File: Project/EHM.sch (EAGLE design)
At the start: 111 parts, among them J1 282834-2, J2 282834-2, J3 282834-2, J4 282834-2, J5 S2B-PH-SM4-TB(LF)(SN), J6 S6B-PH-SM4-TB(LF)(SN), Q1 BC557B, Q2 BC547B, U1 MAX9934TAUA, U2 BQ25570RGRR, U3 TSU111ICT, U4 MAX9934TAUA, U5 TSU111ICT, U6 TSU111ICT

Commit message: Update project to v1.3
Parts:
- added J7: S2B-PH-SM4-TB(LF)(SN), S2B-PH-SM4-TB_LF__SN_:S2B-PH-SM4-TB(LF)(SN)
- C1: value DNP -> 0.01uF; device rcl:C-EUC1210 -> rcl:C-EUC0805
- C10: value (none) -> 0.1uF
- C11: value 0.01uF -> DNP
- C12: value 4.7uF -> 0.1uF
- C13, C9: value 0.1uF -> 4.7uF
- C14: value DNP -> 0.1uF
- C15: value 4.7uF -> DNP
- C17: value 0.1uF -> DNP
- C2, C3: value 0.01uF -> DNP; device rcl:C-EUC0805 -> rcl:C-EUC1210
- C21: value DNP -> 0.1uF; device rcl:C-EUC1812 -> rcl:C-EUC0805
- C22: device rcl:C-EUC0805 -> rcl:C-EUC1812
- C23: device rcl:C-EUC0805 -> rcl:C-EUC0603
- C24, C25: value (none) -> 0.1uF; device rcl:C-EUC0805 -> rcl:C-EUC0603
- C4: value 22uF -> 0.01uF
- C5: value 4.7uF -> 0.01uF
- C6: value 0.1uF -> 22uF
- C7: value DNP -> 4.7uF
- C8: value DNP -> 0.1uF; device rcl:C-EUC1210 -> rcl:C-EUC0805
- J5: value S2B-PH-SM4-TB(LF)(SN) -> 282834-2; device S2B-PH-SM4-TB_LF__SN_:S2B-PH-SM4-TB(LF)(SN) -> 282834-2:282834-2
- R1, R10, R12, R13, R5, R9: value DNP -> (none)
- R11, R3: value DNP -> (none); device rcl:R-EU_R0603 -> Y14870RXX000B9R:Y14870RXX000B9R
- R15, R16, R17, R18, R19, R22, R23: value (none) -> DNP
- R4: device Y14870RXX000B9R:Y14870RXX000B9R -> rcl:R-EU_R0603
- R8: value (none) -> DNP; device Y14870RXX000B9R:Y14870RXX000B9R -> rcl:R-EU_R0603
- SJ1, SJ3, SJ8: device jumper:SJ2W -> jumper:SJ
- SJ13, SJ14, SJ17: device jumper:SJ -> jumper:SJ2W
- TP18: value TPPAD1-13Y -> TPPAD1-13; device testpad:TPPAD1-13Y -> testpad:TPPAD1-13
- TP23: value TPPAD1-13Y -> TPB1,27; device testpad:TPPAD1-13Y -> testpad:TPB1,27
- U1: value MAX9934TAUA -> BQ25570RGRR; device MAX9934TAUA:MAX9934TAUA -> BQ25570RGRR:BQ25570RGRR
- U2: value BQ25570RGRR -> MAX9934TAUA; device BQ25570RGRR:BQ25570RGRR -> MAX9934TAUA:MAX9934TAUA
- U3: value TSU111ICT -> MAX9934TAUA; device TSU111ICT:TSU111ICT -> MAX9934TAUA:MAX9934TAUA
- U4: value MAX9934TAUA -> MAX9620; device MAX9934TAUA:MAX9934TAUA -> MAX9620:MAX9620
- U5, U6: value TSU111ICT -> MAX9620; device TSU111ICT:TSU111ICT -> MAX9620:MAX9620
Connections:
- removed net N$15 (its old number): R5.1, U3.IN-, U3.OUT
- removed net N$19: Q2.C, R10.2, R9.1
- new net N$25: Q2.C, R14.2, R15.1
- new net N$9: R18.1, U4.IN-, U4.OUT
- net CMES1: now also C2.1, C4.1, R1.2, U2.OUT; no longer C11.1, C8.1, R6.2, U4.OUT
- net CMES2: now also C5.1, U3.OUT; no longer C1.1, U1.OUT
- net GND: now also C10.1, C16.2, C17.2, C5.2, C6.2, C7.1, C8.1, C9.1, J5.1, J7.2, J7.SHIELD, R1.1, R13.1, R20.1, R5.1, U1.EP@1, U1.EP@2, U1.EP@3, U1.EP@4, U1.EP@5, U1.NC1, U1.NC2, U1.VSS@1, U1.VSS@2, U2.GROUND, U3.GROUND, U4.VCC-; no longer C10.2, C16.1, C17.1, C5.1, C6.1, C7.2, C8.2, C9.2, J5.2, J5.SHIELD, R12.1, R16.1, R23.1, R3.1, U1.GROUND, U2.EP@1, U2.EP@2, U2.EP@3, U2.EP@4, U2.EP@5, U2.NC1, U2.NC2, U2.VSS@1, U2.VSS@2, U3.VCC-, U4.GROUND
- net LBOOST: now also U1.LBOOST; no longer U2.LBOOST
- net LBUCK: now also U1.LBUCK; no longer U2.LBUCK
- net N$1: now also C18.1, SJ3.1, U2.RSN; no longer C22.1, SJ9.1, U4.RSN
- net N$10: now also C21.1, U3.RSP; no longer C20.1, U1.RSP
- net N$11: now also C19.1, U3.RSN; no longer C18.1, U1.RSN
- net N$12: now also R19.2; no longer C24.1, R20.2
- net N$13: now also R18.2, SJ17.3; no longer C25.1, R21.2, SJ19.3
- net N$14: now also SJ15.2, U4.IN+; no longer SJ12.2, U6.IN+
- net N$16: now also R21.2, SJ19.3; no longer C10.1, R5.2, SJ3.3
- net N$17: now also R16.2, R17.2, SJ14.1, U6.IN+; no longer R1.2, R3.2, SJ1.1, U3.IN+
- net N$18: now also R16.1, SJ14.3; no longer R1.1, SJ1.3
- net N$2: now also R20.2, R22.1; no longer R12.2, R13.1
- net N$20: now also R15.2; no longer R9.2
- net N$21: now also SJ13.3; no longer SJ8.3
- net N$23: now also R14.1; no longer R10.1
- net N$3: now also R22.2, R23.1; no longer R13.2, R14.1
- net N$4: now also R7.2, U2.CS; no longer R11.2, U4.CS
- net N$5: now also R19.1; no longer R20.1
- net N$6: now also C20.1, SJ5.1, U2.RSP; no longer C23.1, SJ10.1, U4.RSP
- net N$7: now also R8.2, U3.CS; no longer R7.2, U1.CS
- net N$8: now also SJ16.2; no longer SJ11.2
- net NEN: now also U1.!EN; no longer U2.!EN
- net OK_HYST: now also R10.2, R9.1, U1.OK_HYST; no longer R18.1, R19.2, U2.OK_HYST
- net OK_PROG: now also R10.1, R6.2, U1.OK_PROG; no longer R17.2, R19.1, U2.OK_PROG
- net RSN2: now also J3.2, R3.2, SJ1.2, SJ13.1, SJ15.1, SJ17.1; no longer J2.2, R4.2, SJ12.1, SJ19.1, SJ2.2, SJ8.1
- net RSN2_BUF: now also SJ17.2; no longer SJ19.2
- net RSP1: now also J2.2, R11.2, SJ16.1, SJ2.2; no longer J3.2, R8.2, SJ10.2, SJ11.1
- net SW: now also J7.1; no longer J5.1
- net VBAT: now also C22.1, SJ14.2, SJ19.1, U1.VBAT; no longer C21.1, SJ1.2, SJ3.1, U2.VBAT
- net VBAT_BUF: now also SJ19.2; no longer SJ3.2
- net VBAT_OK: now also U1.VBAT_OK; no longer U2.VBAT_OK
- net VBAT_OV: now also R4.1, R5.2, U1.VBAT_OV; no longer R15.1, R16.2, U2.VBAT_OV
- net VCC_SW: now also J5.2, SJ10.1, SJ11.1, SJ12.1, SJ13.2, SJ8.1, SJ9.1; no longer SJ13.1, SJ14.1, SJ15.1, SJ16.1, SJ17.1, SJ8.2
- net VCC_SW1: now also C7.2, C8.2, R7.1, SJ8.2, U2.VCC; no longer C16.2, C17.2, R11.1, SJ13.2, U4.VCC
- net VCC_SW2: now also C10.2, C9.2, R8.1, SJ9.2, U3.VCC; no longer C5.2, C6.2, R7.1, SJ14.2, U1.VCC
- net VCC_SW3: now also C24.1, SJ10.2; no longer SJ15.2
- net VCC_SW4: now also C23.1, SJ11.2, U4.VCC+; no longer SJ16.2, U6.VCC+
- net VCC_SW5: now also C25.1, SJ12.2, U6.VCC+; no longer SJ17.2, U3.VCC+
- net VIN_DC: now also C14.1, C16.1, C17.1, R11.1, R23.2, SJ2.1, SJ3.2, U1.VIN_DC; no longer C13.1, C15.1, C19.1, R14.2, R8.1, SJ5.1, SJ9.2, U2.VIN_DC
- net VOC_SAMP: now also U1.VOC_SAMP; no longer U2.VOC_SAMP
- net VOUT: now also C11.1, C6.1, R3.1, SJ1.1, U1.VOUT; no longer C4.1, C7.1, R4.1, SJ2.1, U2.VOUT
- net VOUT_EN: now also U1.VOUT_EN; no longer U2.VOUT_EN
- net VOUT_SET: now also R12.1, R13.2, U1.VOUT_SET; no longer R22.1, R23.2, U2.VOUT_SET
- net VRDIV: now also R12.2, R4.2, R9.2, U1.VRDIV; no longer R15.2, R18.2, R22.2, U2.VRDIV
- net VREF_SAMP: now also C1.1, U1.VREF_SAMP; no longer C2.1, U2.VREF_SAMP
- net VSTOR: now also C13.1, C15.1, U1.VSTOR; no longer C14.1, C9.1, U2.VSTOR
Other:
- moved on the sheet: C1, C10, C11, C12, C13, C14, C15, C16, C17, C18, C19, C2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

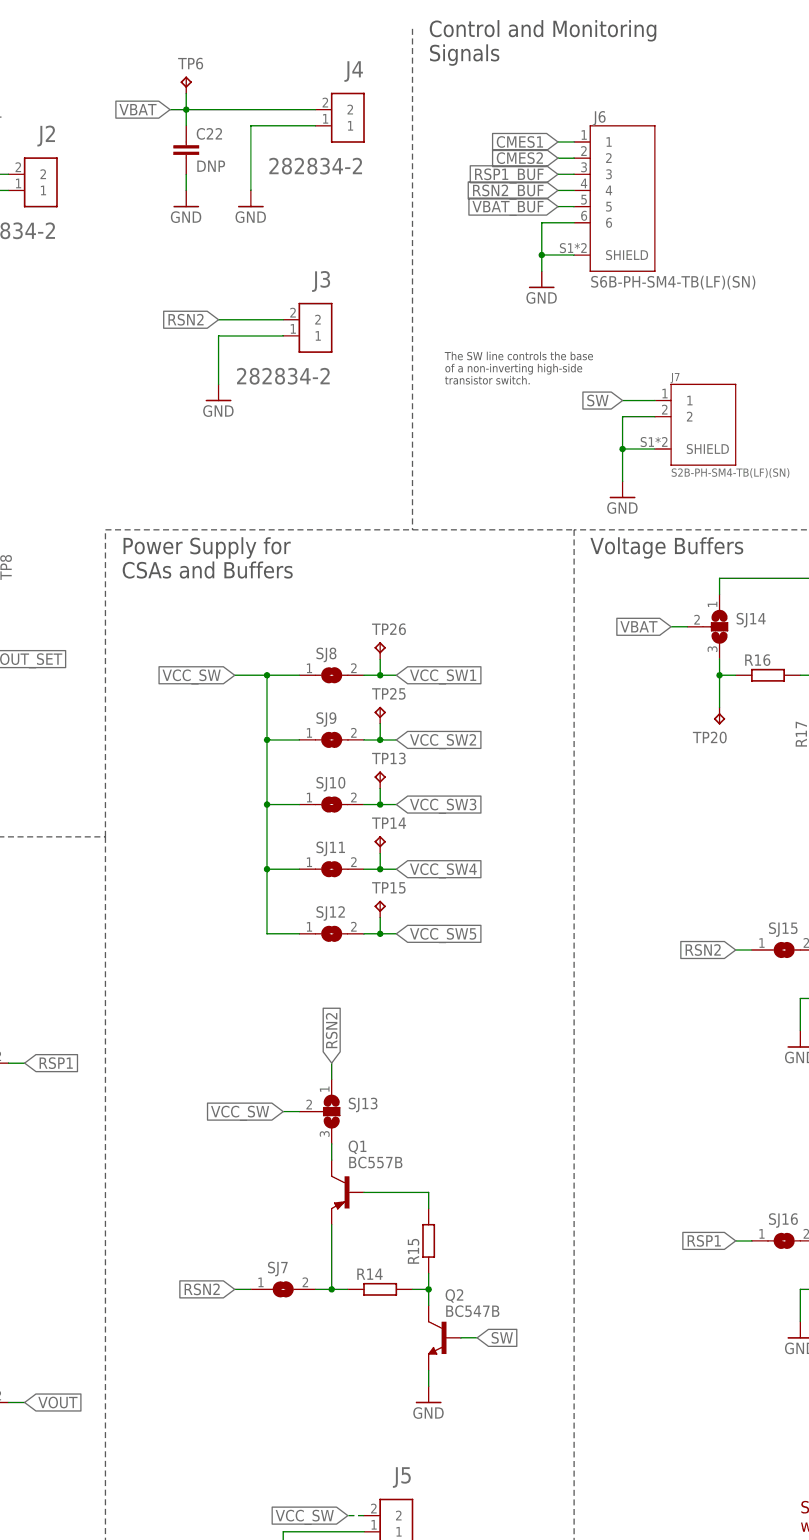
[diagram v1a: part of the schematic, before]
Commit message: Added resistor to base of high side switch
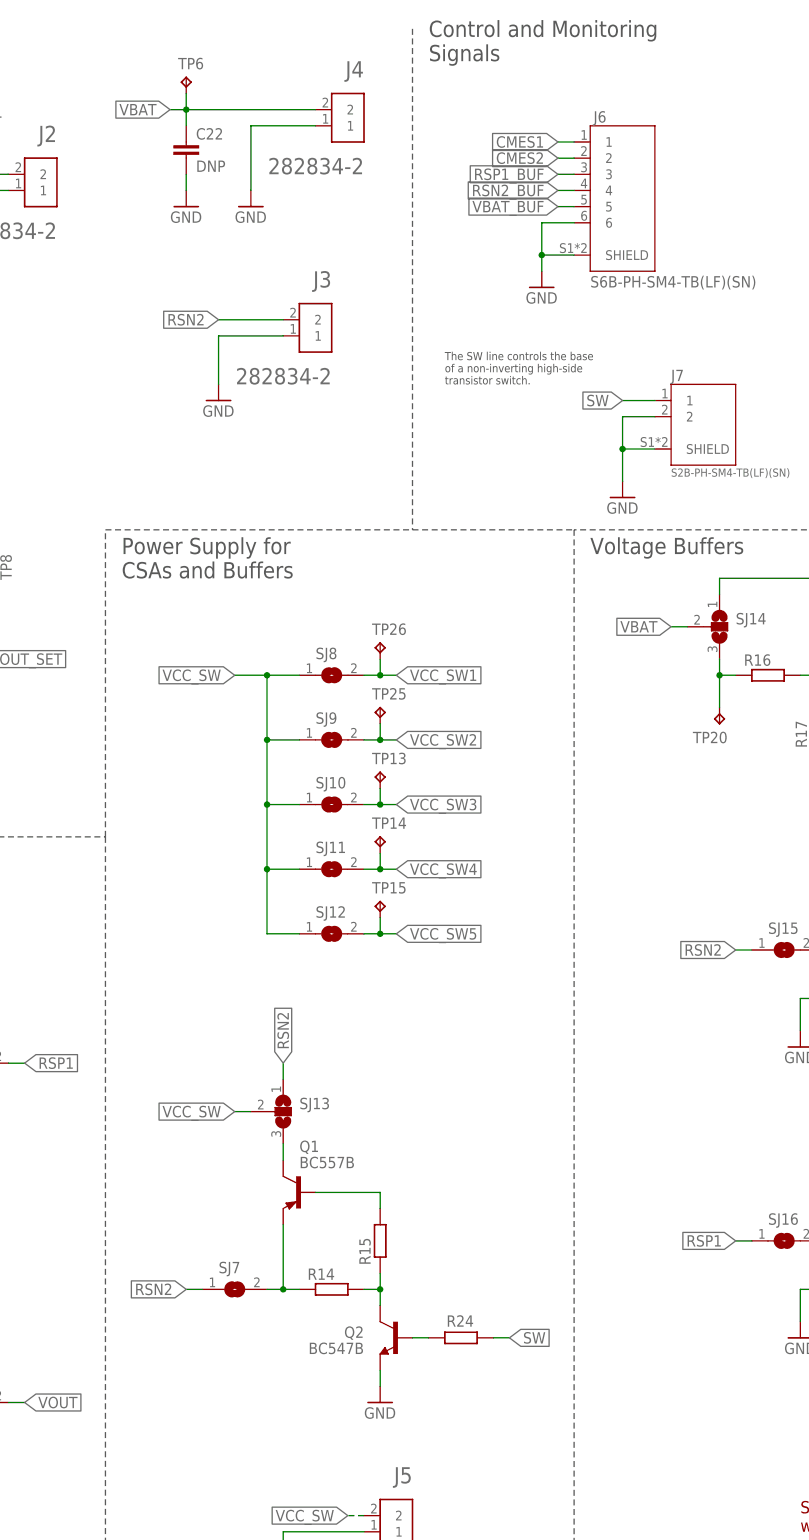
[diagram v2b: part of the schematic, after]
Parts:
- added R24: DNP, rcl:R-EU_R0603
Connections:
- new net N$19: Q2.B, R24.1
- net SW: now also R24.2; no longer Q2.B
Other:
- moved on the sheet: Q1, Q2, R14, R15, SJ13, SJ7
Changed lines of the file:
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@@
 <part name="J5" library="282834-2" deviceset="282834-2" device=""/>
 <part name="GND24" library="supply1" library_urn="urn:adsk.eagle:library:371" deviceset="GND" device=""/>
+<part name="R24" library="rcl" library_urn="urn:adsk.eagle:library:334" deviceset="R-EU_" device="R0603" package3d_urn="urn:adsk.eagle:package:23555/2" value="DNP"/>
 </parts>
 <sheets>
@@
 </instance>
 <instance part="J6" gate="G$1" x="261.62" y="228.6" smashed="yes">
-<attribute name="NAME" x="257.0465" y="239.2715" size="1.77858125" layer="95"/>
+<attribute name="NAME" x="257.0465" y="239.2715" size="1.778" layer="95"/>
 <attribute name="VALUE" x="256.5373" y="213.3519" size="1.778940625" layer="96"/>
 </instance>
@@
 <attribute name="NAME" x="280.67" y="153.8986" size="1.778" layer="95"/>
 </instance>
-<instance part="Q1" gate="G$1" x="218.44" y="71.12" smashed="yes" rot="R180">
-<attribute name="NAME" x="218.44" y="77.47" size="1.778" layer="95"/>
-<attribute name="VALUE" x="218.44" y="74.93" size="1.778" layer="96"/>
+<instance part="Q1" gate="G$1" x="210.82" y="71.12" smashed="yes" rot="R180">
+<attribute name="NAME" x="210.82" y="77.47" size="1.778" layer="95"/>
+<attribute name="VALUE" x="210.82" y="74.93" size="1.778" layer="96"/>
 </instance>
 <instance part="J7" gate="G$1" x="274.32" y="193.04" smashed="yes">
-<attribute name="NAME" x="269.2371" y="198.63571875" size="1.272509375" layer="95"/>
+<attribute name="NAME" x="269.2371" y="198.63571875" size="1.778" layer="95"/>
 <attribute name="VALUE" x="269.23188125" y="183.61731875" size="1.275409375" layer="96"/>
 </instance>
@@
 <attribute name="VALUE" x="259.08" y="177.8" size="1.778" layer="96"/>
 </instance>
-<instance part="Q2" gate="G$1" x="233.68" y="48.26" smashed="yes" rot="MR0">
-<attribute name="NAME" x="233.68" y="55.88" size="1.778" layer="95" rot="MR180"/>
-<attribute name="VALUE" x="233.68" y="53.34" size="1.778" layer="96" rot="MR180"/>
-</instance>
-<instance part="R15" gate="G$1" x="231.14" y="63.5" smashed="yes" rot="R90">
-<attribute name="NAME" x="229.6414" y="59.69" size="1.778" layer="95" rot="R90"/>
-</instance>
-<instance part="R14" gate="G$1" x="223.52" y="55.88" smashed="yes">
-<attribute name="NAME" x="219.71" y="57.3786" size="1.778" layer="95"/>
-</instance>
-<instance part="GND25" gate="1" x="231.14" y="38.1" smashed="yes">
-<attribute name="VALUE" x="228.6" y="35.56" size="1.778" layer="96"/>
-</instance>
-<instance part="SJ13" gate="G$1" x="215.9" y="83.82" smashed="yes">
-<attribute name="NAME" x="218.44" y="84.201" size="1.778" layer="95"/>
-<attribute name="VALUE" x="218.44" y="81.915" size="1.778" layer="96"/>
-</instance>
-<instance part="SJ7" gate="1" x="208.28" y="55.88" smashed="yes">
-<attribute name="NAME" x="205.74" y="58.42" size="1.778" layer="95"/>
-<attribute name="VALUE" x="205.74" y="52.07" size="1.778" layer="96"/>
+<instance part="Q2" gate="G$1" x="226.06" y="48.26" smashed="yes" rot="MR0">
+<attribute name="NAME" x="220.98" y="48.26" size="1.778" layer="95" rot="MR0"/>
+<attribute name="VALUE" x="220.98" y="45.72" size="1.778" layer="96" rot="MR0"/>
+</instance>
+<instance part="R15" gate="G$1" x="223.52" y="63.5" smashed="yes" rot="R90">
+<attribute name="NAME" x="222.0214" y="59.69" size="1.778" layer="95" rot="R90"/>
+</instance>
+<instance part="R14" gate="G$1" x="215.9" y="55.88" smashed="yes">
+<attribute name="NAME" x="212.09" y="57.3786" size="1.778" layer="95"/>
+</instance>
+<instance part="GND25" gate="1" x="223.52" y="38.1" smashed="yes">
+<attribute name="VALUE" x="220.98" y="35.56" size="1.778" layer="96"/>
+</instance>
+<instance part="SJ13" gate="G$1" x="208.28" y="83.82" smashed="yes">
+<attribute name="NAME" x="210.82" y="84.201" size="1.778" layer="95"/>
+<attribute name="VALUE" x="210.82" y="81.915" size="1.778" layer="96"/>
+</instance>
+<instance part="SJ7" gate="1" x="200.66" y="55.88" smashed="yes">
+<attribute name="NAME" x="198.12" y="58.42" size="1.778" layer="95"/>
+<attribute name="VALUE" x="198.12" y="52.07" size="1.778" layer="96"/>
 </instance>
 <instance part="TP12" gate="G$1" x="114.3" y="215.9" smashed="yes" rot="R90">
@@
 <instance part="GND24" gate="1" x="208.28" y="12.7" smashed="yes">
 <attribute name="VALUE" x="205.74" y="10.16" size="1.778" layer="96"/>
+</instance>
+<instance part="R24" gate="G$1" x="236.22" y="48.26" smashed="yes">
+<attribute name="NAME" x="233.934" y="50.0126" size="1.778" layer="95"/>
 </instance>
 </instances>
@@
 <pinref part="GND25" gate="1" pin="GND"/>
 <pinref part="Q2" gate="G$1" pin="E"/>
-<wire x1="231.14" y1="40.64" x2="231.14" y2="43.18" width="0.1524" layer="91"/>
+<wire x1="223.52" y1="40.64" x2="223.52" y2="43.18" width="0.1524" layer="91"/>
 </segment>
 </net>
@@
 <segment>
 <pinref part="SJ13" gate="G$1" pin="2"/>
-<wire x1="210.82" y1="83.82" x2="208.28" y2="83.82" width="0.1524" layer="91"/>
-<label x="208.28" y="83.82" size="1.778" layer="95" rot="R180" xref="yes"/>
+<wire x1="203.2" y1="83.82" x2="200.66" y2="83.82" width="0.1524" layer="91"/>
+<label x="200.66" y="83.82" size="1.778" layer="95" rot="R180" xref="yes"/>
 </segment>
 <segment>
@@
 <segment>
 <pinref part="SJ13" gate="G$1" pin="1"/>
-<wire x1="215.9" y1="88.9" x2="215.9" y2="91.44" width="0.1524" layer="91"/>
-<label x="215.9" y="91.44" size="1.778" layer="95" rot="R90" xref="yes"/>
+<wire x1="208.28" y1="88.9" x2="208.28" y2="91.44" width="0.1524" layer="91"/>
+<label x="208.28" y="91.44" size="1.778" layer="95" rot="R90" xref="yes"/>
 </segment>
 <segment>
 <pinref part="SJ7" gate="1" pin="1"/>
-<wire x1="203.2" y1="55.88" x2="200.66" y2="55.88" width="0.1524" layer="91"/>
-<label x="200.66" y="55.88" size="1.778" layer="95" rot="R180" xref="yes"/>
+<wire x1="195.58" y1="55.88" x2="193.04" y2="55.88" width="0.1524" layer="91"/>
+<label x="193.04" y="55.88" size="1.778" layer="95" rot="R180" xref="yes"/>
 </segment>
 </net>
@@
 <segment>
 <pinref part="R15" gate="G$1" pin="2"/>
-<wire x1="231.14" y1="68.58" x2="231.14" y2="71.12" width="0.1524" layer="91"/>
+<wire x1="223.52" y1="68.58" x2="223.52" y2="71.12" width="0.1524" layer="91"/>
 <pinref part="Q1" gate="G$1" pin="B"/>
-<wire x1="231.14" y1="71.12" x2="220.98" y2="71.12" width="0.1524" layer="91"/>
+<wire x1="223.52" y1="71.12" x2="213.36" y2="71.12" width="0.1524" layer="91"/>
 </segment>
 </net>
@@
 </segment>
 <segment>
-<pinref part="Q2" gate="G$1" pin="B"/>
-<wire x1="236.22" y1="48.26" x2="238.76" y2="48.26" width="0.1524" layer="91"/>
-<label x="238.76" y="48.26" size="1.778" layer="95" xref="yes"/>
+<pinref part="R24" gate="G$1" pin="2"/>
+<wire x1="241.3" y1="48.26" x2="243.84" y2="48.26" width="0.1524" layer="91"/>
+<label x="243.84" y="48.26" size="1.778" layer="95" xref="yes"/>
 </segment>
 </net>
@@
 <pinref part="Q1" gate="G$1" pin="C"/>
 <pinref part="SJ13" gate="G$1" pin="3"/>
-<wire x1="215.9" y1="76.2" x2="215.9" y2="78.74" width="0.1524" layer="91"/>
+<wire x1="208.28" y1="76.2" x2="208.28" y2="78.74" width="0.1524" layer="91"/>
 </segment>
 </net>
@@
 <segment>
 <pinref part="Q1" gate="G$1" pin="E"/>
-<wire x1="215.9" y1="66.04" x2="215.9" y2="55.88" width="0.1524" layer="91"/>
+<wire x1="208.28" y1="66.04" x2="208.28" y2="55.88" width="0.1524" layer="91"/>
 <pinref part="SJ7" gate="1" pin="2"/>
-<wire x1="213.36" y1="55.88" x2="215.9" y2="55.88" width="0.1524" layer="91"/>
+<wire x1="205.74" y1="55.88" x2="208.28" y2="55.88" width="0.1524" layer="91"/>
 <pinref part="R14" gate="G$1" pin="1"/>
-<wire x1="218.44" y1="55.88" x2="215.9" y2="55.88" width="0.1524" layer="91"/>
-<junction x="215.9" y="55.88"/>
+<wire x1="210.82" y1="55.88" x2="208.28" y2="55.88" width="0.1524" layer="91"/>
+<junction x="208.28" y="55.88"/>
 </segment>
 </net>
@@
 <segment>
 <pinref part="R15" gate="G$1" pin="1"/>
-<wire x1="231.14" y1="55.88" x2="231.14" y2="58.42" width="0.1524" layer="91"/>
+<wire x1="223.52" y1="55.88" x2="223.52" y2="58.42" width="0.1524" layer="91"/>
 <pinref part="R14" gate="G$1" pin="2"/>
-<wire x1="228.6" y1="55.88" x2="231.14" y2="55.88" width="0.1524" layer="91"/>
+<wire x1="220.98" y1="55.88" x2="223.52" y2="55.88" width="0.1524" layer="91"/>
 <pinref part="Q2" gate="G$1" pin="C"/>
-<wire x1="231.14" y1="53.34" x2="231.14" y2="55.88" width="0.1524" layer="91"/>
-<junction x="231.14" y="55.88"/>
-</segment>
-</net>
+<wire x1="223.52" y1="53.34" x2="223.52" y2="55.88" width="0.1524" layer="91"/>
+<junction x="223.52" y="55.88"/>
+</segment>
+</net>
+<net name="N$19" class="0">
+<segment>
+<pinref part="R24" gate="G$1" pin="1"/>
+<pinref part="Q2" gate="G$1" pin="B"/>
+<wire x1="231.14" y1="48.26" x2="228.6" y2="48.26" width="0.1524" layer="91"/>
+</segment>
+</net>

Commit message: Updated to V1.4
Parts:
- added R25: 0R, rcl:R-EU_R0603
- added R26: 7.87M, rcl:R-EU_R0603
- added TP27: TPB1,27, testpad:TPB1,27
- R1: value (none) -> 10.7k
- R10, R12: value (none) -> 7.15M
- R11: value (none) -> 0.05R
- R13: value (none) -> 5.76M
- R14, R7, R8: value DNP -> 10k
- R15: value DNP -> 2.2k
- R16: value DNP -> 18k
- R17, R18, R19, R20: value DNP -> 10M
- R2: value (none) -> 9.31k
- R21: value DNP -> 5.23M
- R22, R23, R24: value DNP -> 0R
- R3: value (none) -> 0.1R
- R4: value (none) -> 7.32M
- R5: value (none) -> 5.62M
- R6: value (none) -> 5.11M
- R9: value (none) -> 866k
- SJ13: device jumper:SJ2W -> jumper:SJ
- SJ15, SJ8: device jumper:SJ -> jumper:SJ2W
- TP11, TP16: value TPPAD1-13Y -> TPPAD1-13; device testpad:TPPAD1-13Y -> testpad:TPPAD1-13
- TP19: value TPPAD1-13Y -> TPB1,27; device testpad:TPPAD1-13Y -> testpad:TPB1,27
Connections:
- new net N$26: R18.1, SJ15.3, TP27.TP
- net GND: now also R19.1, R21.1; no longer R17.1
- net N$12: now also R23.2; no longer R19.2
- net N$13: now also R24.2, SJ19.3; no longer R18.2, SJ17.3
- net N$14: now also SJ16.2, U6.IN+; no longer SJ15.2, U4.IN+
- net N$15: now also R22.1, U4.IN-, U4.OUT; no longer R21.1, U6.IN-, U6.OUT
- net N$16: now also R22.2, SJ17.3; no longer R21.2, SJ19.3
- net N$17: now also R19.2, U4.IN+; no longer R16.2, U6.IN+
- net N$18: now also R17.1; no longer R16.1
- net N$19: now also R16.1; no longer R24.1
- net N$2: now also R21.2, R25.1; no longer R20.2, R22.1
- net N$21: now also SJ8.3; no longer SJ13.3
- net N$3: now also R25.2, R26.1; no longer R22.2, R23.1
- net N$5: now also R23.1; no longer R19.1
- net N$8: now also R18.2, R20.2, SJ15.1; no longer SJ16.2
- net N$9: now also R24.1, U6.IN-, U6.OUT; no longer R18.1, U4.IN-, U4.OUT
- net RSN2: now also SJ16.1, SJ19.1, SJ8.1; no longer SJ13.1, SJ15.1, SJ17.1
- net RSN2_BUF: now also SJ19.2; no longer SJ17.2
- net RSP1: now also SJ15.2; no longer SJ16.1
- net SW: now also R16.2; no longer R24.2
- net VBAT: now also SJ17.1; no longer SJ19.1
- net VBAT_BUF: now also SJ17.2; no longer SJ19.2
- net VCC_SW: now also SJ13.1, SJ8.2; no longer SJ13.2, SJ8.1
- net VCC_SW1: now also SJ9.2; no longer SJ8.2
- net VCC_SW2: now also SJ10.2; no longer SJ9.2
- net VCC_SW3: now also SJ11.2; no longer SJ10.2
- net VCC_SW4: now also C25.1, SJ12.2, U6.VCC+; no longer C23.1, SJ11.2, U4.VCC+
- net VCC_SW5: now also C23.1, SJ13.2, U4.VCC+; no longer C25.1, SJ12.2, U6.VCC+
- net VIN_DC: now also R26.2; no longer R23.2
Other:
- moved on the sheet: C23, C24, C25, R16, R17, R18, R19, R20, R21, R22, R23, R24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
